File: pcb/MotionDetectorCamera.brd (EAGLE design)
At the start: 55.9 x 44.5 mm, 130 parts, among them J2 S-MOUNT-LENS-HOLDER, U1 LATTICE-ICE40HX4K-BG121, U10 NXP-NTB0102, U11 ON-NLAS3157, U12 ON-NLAS3157, U13 STM-STM32F730, U2 TI-TPS6280XYKAR, U3 MICROSD-SOCKET, U4 TI-TPS6280XYKAR, U5 W989D6DBGX6I, U6 TI-TPS63805YFFR, U8 ON-AR0330CS1C12SPKA0, U9 TI-TMUX1574, X1 SITIME-SIT8021, X2 SITIME-SIT8021

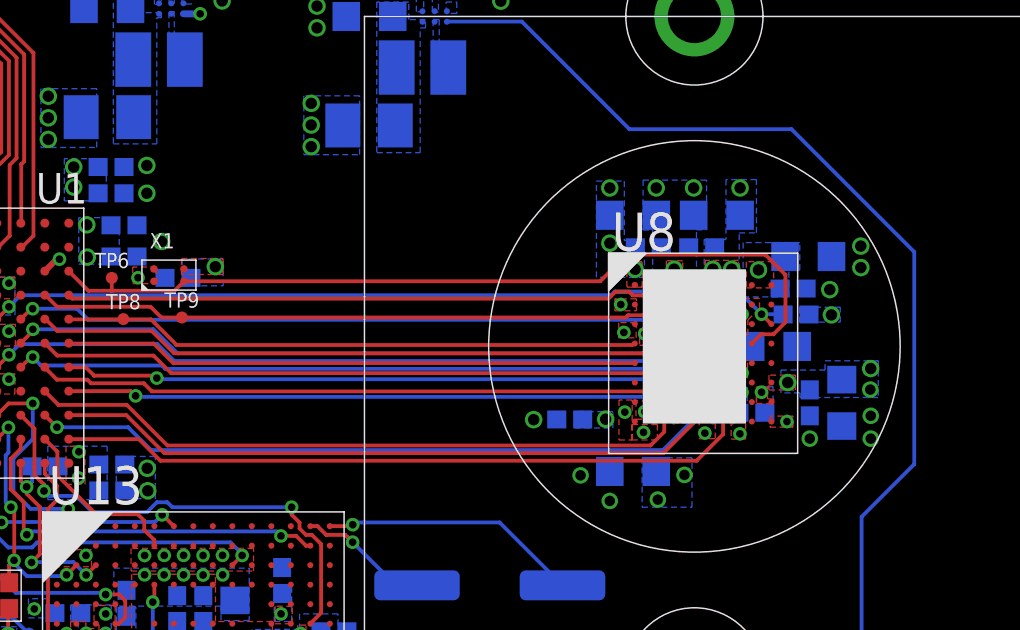
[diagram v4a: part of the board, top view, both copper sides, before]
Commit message: Add pullup for PIX_SDATA
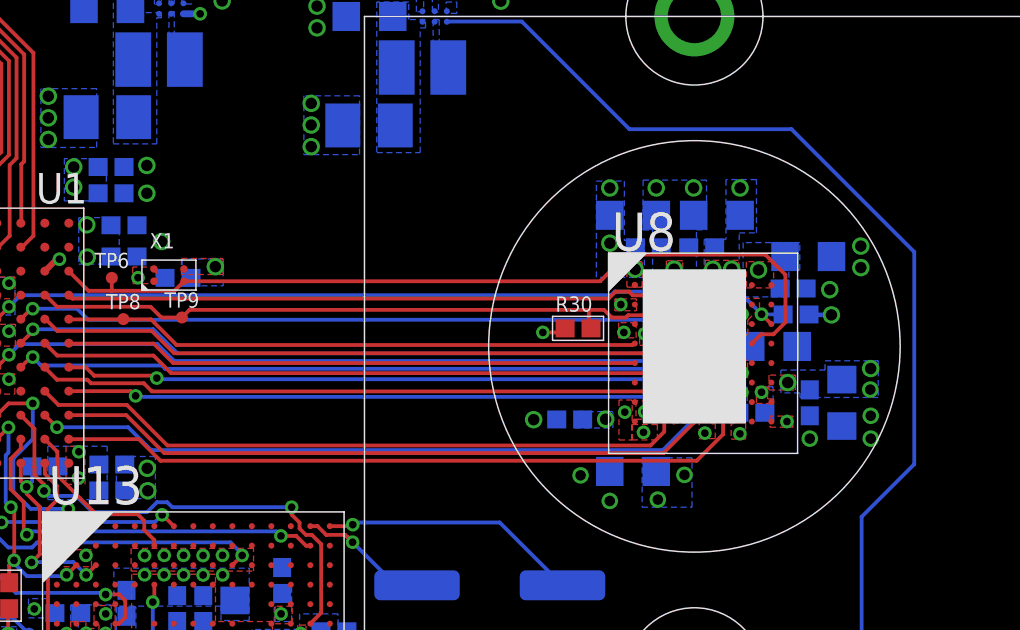
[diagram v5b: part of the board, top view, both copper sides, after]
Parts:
- added R30: 4.7k, EagleLibrary:0402
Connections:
- net 1V8: now also R30.1
- net PIX_SDATA: now also R30.2
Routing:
- net 1V8: track 4.92 -> 6.47 mm, vias 70 -> 71
- net PIX_SDATA: track 20.8 -> 21.7 mm
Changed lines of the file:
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@@
 <attribute name="PN" value="CRCW040210K0FKEDC" x="19.286221875" y="18.8950625" size="1.778" layer="27" rot="R90" display="off"/>
+</element>
+<element name="R30" library="EagleLibrary" package="0402" package3d_urn="urn:adsk.eagle:package:17080064/1" value="4.7k" x="38.249859375" y="27.805378125" smashed="yes">
+<attribute name="MFG" value="" x="38.249859375" y="27.805378125" size="1.778" layer="27" display="off"/>
+<attribute name="NAME" x="37.495859375" y="28.361378125" size="0.508" layer="25" font="vector"/>
+<attribute name="PN" value="" x="38.249859375" y="27.805378125" size="1.778" layer="27" display="off"/>
 </element>
 </elements>
@@
 </polygon>
 <polygon width="0.127" layer="16" thermals="no">
-<vertex x="45.63618125" y="28.508959375"/>
-<vertex x="45.63618125" y="28.0136625"/>
-<vertex x="46.99" y="28.0136625"/>
-<vertex x="46.99" y="28.508959375"/>
-</polygon>
-<polygon width="0.127" layer="16" thermals="no">
 <vertex x="40.386" y="23.492459375"/>
 <vertex x="40.386" y="21.844"/>
@@
 <wire x1="16.17345" y1="19.9905" x2="16.17345" y2="20.6082875" width="0.127" layer="16"/>
 <wire x1="16.17345" y1="20.6082875" x2="16.11121875" y2="20.67051875" width="0.127" layer="16"/>
+<contactref element="R30" pad="1"/>
+<wire x1="45.9493" y1="28.2702" x2="45.964540625" y2="28.254959375" width="0.1524" layer="16"/>
+<wire x1="45.964540625" y1="28.254959375" x2="46.695359375" y2="28.254959375" width="0.1524" layer="16"/>
+<via x="37.076378125" y="27.670759375" extent="1-16" drill="0.254"/>
+<wire x1="37.817359375" y1="27.805378125" x2="37.682740625" y2="27.670759375" width="0.127" layer="1"/>
+<wire x1="37.682740625" y1="27.670759375" x2="37.076378125" y2="27.670759375" width="0.127" layer="1"/>
 </signal>
 <signal name="GND">
@@
 <signal name="PIX_RST_">
 <contactref element="U8" pad="C8"/>
-<wire x1="44.693" y1="27.9498" x2="44.366178125" y2="28.276621875" width="0.127" layer="1"/>
-<wire x1="44.366178125" y1="28.27781875" x2="44.366178125" y2="28.276621875" width="0.127" layer="1"/>
 <via x="44.366178125" y="28.27781875" extent="1-16" drill="0.254"/>
 <wire x1="39.4716" y1="29.0322" x2="43.6112125" y2="29.0322" width="0.127" layer="16"/>
@@
 <wire x1="19.66468125" y1="28.91028125" x2="39.34968125" y2="28.91028125" width="0.127" layer="16"/>
 <contactref element="R23" pad="1"/>
-<wire x1="44.366178125" y1="28.27781875" x2="45.07668125" y2="28.27781875" width="0.127" layer="16"/>
-<wire x1="45.07668125" y1="28.27781875" x2="45.0843" y2="28.2702" width="0.127" layer="16"/>
+<wire x1="45.0843" y1="28.2702" x2="44.373796875" y2="28.2702" width="0.127" layer="16"/>
+<wire x1="44.373796875" y1="28.2702" x2="44.366178125" y2="28.27781875" width="0.127" layer="16"/>
+<wire x1="44.693" y1="27.9498" x2="44.366178125" y2="28.276621875" width="0.127" layer="1"/>
+<wire x1="44.366178125" y1="28.276621875" x2="44.366178125" y2="28.27781875" width="0.127" layer="1"/>
 </signal>
 <signal name="PIX_SCLK">
@@
 <contactref element="U8" pad="B2"/>
 <wire x1="39.92040625" y1="28.2419" x2="39.84710625" y2="28.1686" width="0.127" layer="1"/>
-<wire x1="39.84710625" y1="28.1686" x2="25.0444" y2="28.1686" width="0.127" layer="1"/>
+<wire x1="39.84710625" y1="28.1686" x2="39.37" y2="28.1686" width="0.127" layer="1"/>
+<wire x1="39.116" y1="28.4226" x2="38.608" y2="28.4226" width="0.127" layer="1"/>
+<wire x1="38.608" y1="28.4226" x2="25.2984" y2="28.4226" width="0.127" layer="1"/>
+<wire x1="25.2984" y1="28.4226" x2="25.0444" y2="28.1686" width="0.127" layer="1"/>
+<wire x1="39.37" y1="28.1686" x2="39.116" y2="28.4226" width="0.127" layer="1"/>
 <wire x1="25.0444" y1="28.1686" x2="24.3586" y2="28.1686" width="0.127" layer="1"/>
 <wire x1="40.793" y1="28.5998" x2="40.4351" y2="28.2419" width="0.127" layer="1"/>
@@
 <wire x1="20.8833" y1="28.5249" x2="24.0023" y2="28.5249" width="0.127" layer="1"/>
 <contactref element="TP9" pad="X"/>
+<contactref element="R30" pad="2"/>
+<wire x1="38.682359375" y1="27.805378125" x2="38.608" y2="27.8797375" width="0.127" layer="1"/>
+<wire x1="38.608" y1="27.8797375" x2="38.608" y2="28.4226" width="0.127" layer="1"/>
 </signal>
 <signal name="2V8GOOD">

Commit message: Remove 3d packages to fix ERC errors
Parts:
- C28, C29: device EagleLibrary:0805@1 -> EagleLibrary:0805

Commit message: Update TI parts with TI- prefix
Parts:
- U2, U4: device EagleLibrary:TPS6280XYKAR -> EagleLibrary:TI-TPS6280XYKAR
- U6: device EagleLibrary:TPS63805YFFR -> EagleLibrary:TI-TPS63805YFFR
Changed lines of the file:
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@@
 <attribute name="PN" value="CR0402-FX-9102GLF" x="45.936" y="8.4582" size="1.778" layer="28" rot="MR90" display="off"/>
 </element>
-<element name="U2" library="EagleLibrary" package="TPS6280XYKAR" value="TI-TPS6280XYKAR" x="24.6888" y="38.4657625" smashed="yes" rot="MR270">
+<element name="U2" library="EagleLibrary" package="TI-TPS6280XYKAR" value="TI-TPS6280XYKAR" x="24.6888" y="38.4657625" smashed="yes" rot="MR270">
 <attribute name="MFG" value="Texas Instruments" x="24.6888" y="38.4657625" size="1.778" layer="28" rot="MR270" display="off"/>
 <attribute name="NAME" x="24.992321875" y="37.939353125" size="0.508" layer="26" font="vector" rot="SMR270"/>
 <attribute name="PN" value="TPS62801YKAR" x="24.6888" y="38.4657625" size="1.778" layer="28" rot="MR270" display="off"/>
 </element>
-<element name="U4" library="EagleLibrary" package="TPS6280XYKAR" value="TI-TPS6280XYKAR" x="33.469578125" y="38.2016" smashed="yes" rot="MR270">
+<element name="U4" library="EagleLibrary" package="TI-TPS6280XYKAR" value="TI-TPS6280XYKAR" x="33.469578125" y="38.2016" smashed="yes" rot="MR270">
 <attribute name="MFG" value="Texas Instruments" x="33.469578125" y="38.2016" size="1.778" layer="28" rot="MR270" display="off"/>
 <attribute name="NAME" x="34.3515875" y="38.665140625" size="0.508" layer="26" font="vector" rot="SMR180"/>
 <attribute name="PN" value="TPS62802YKAR" x="85.539578125" y="8.9916" size="1.778" layer="28" rot="MR270" display="off"/>
 </element>
-<element name="U6" library="EagleLibrary" package="TPS63805YFFR" value="TI-TPS63805YFFR" x="48.2854" y="8.1026" smashed="yes" rot="MR180">
+<element name="U6" library="EagleLibrary" package="TI-TPS63805YFFR" value="TI-TPS63805YFFR" x="48.2854" y="8.1026" smashed="yes" rot="MR180">
 <attribute name="MFG" value="Texas Instruments" x="48.2854" y="8.1026" size="1.778" layer="28" rot="MR180" display="off"/>
 <attribute name="NAME" x="50.09898125" y="8.56668125" size="0.508" layer="26" font="vector" rot="MR270"/>
@@
 <vertex x="25.6286" y="35.9003625"/>
 </polygon>
+<wire x1="25.1423" y1="36.7639625" x2="24.6888" y2="38.2907625" width="0" layer="19" extent="16-16"/>
 </signal>
 <signal name="1V2">
@@
 <vertex x="34.460178125" y="35.6362"/>
 </polygon>
+<wire x1="33.923078125" y1="36.4998" x2="33.469578125" y2="38.0266" width="0" layer="19" extent="16-16"/>
 </signal>
 <signal name="2V8">
@@
 </polygon>
 <wire x1="48.2854" y1="7.7026" x2="48.6854" y2="7.7026" width="0.254" layer="16"/>
+<wire x1="50.7238" y1="7.2681" x2="48.6854" y2="7.7026" width="0" layer="19" extent="16-16"/>
 </signal>
 <signal name="N$13">
@@
 </polygon>
 <wire x1="48.2854" y1="8.5026" x2="48.6854" y2="8.5026" width="0.254" layer="16"/>
+<wire x1="48.6854" y1="8.5026" x2="50.7238" y2="8.9879" width="0" layer="19" extent="16-16"/>
 </signal>
 <signal name="N$11">
@@
 <vertex x="47.1424" y="9.271"/>
 </polygon>
+<wire x1="46.7996" y1="8.9655" x2="45.936" y2="8.8907" width="0" layer="19" extent="16-16"/>
 </signal>
 <signal name="GNDPLL1">

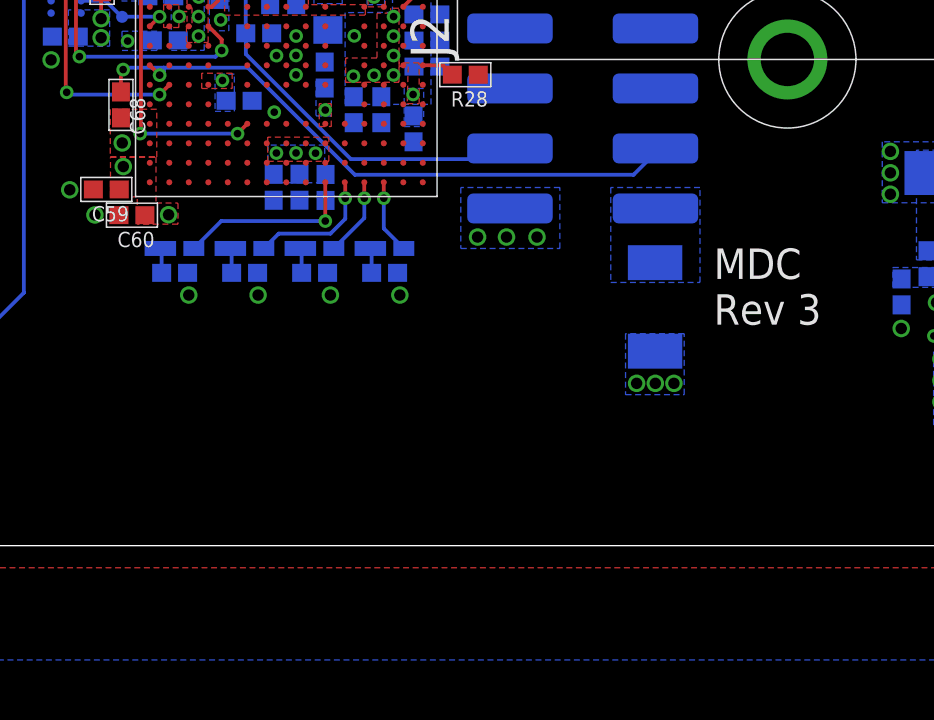
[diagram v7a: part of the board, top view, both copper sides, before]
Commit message: Added USB port, USB ESD chip, and ferrite bead
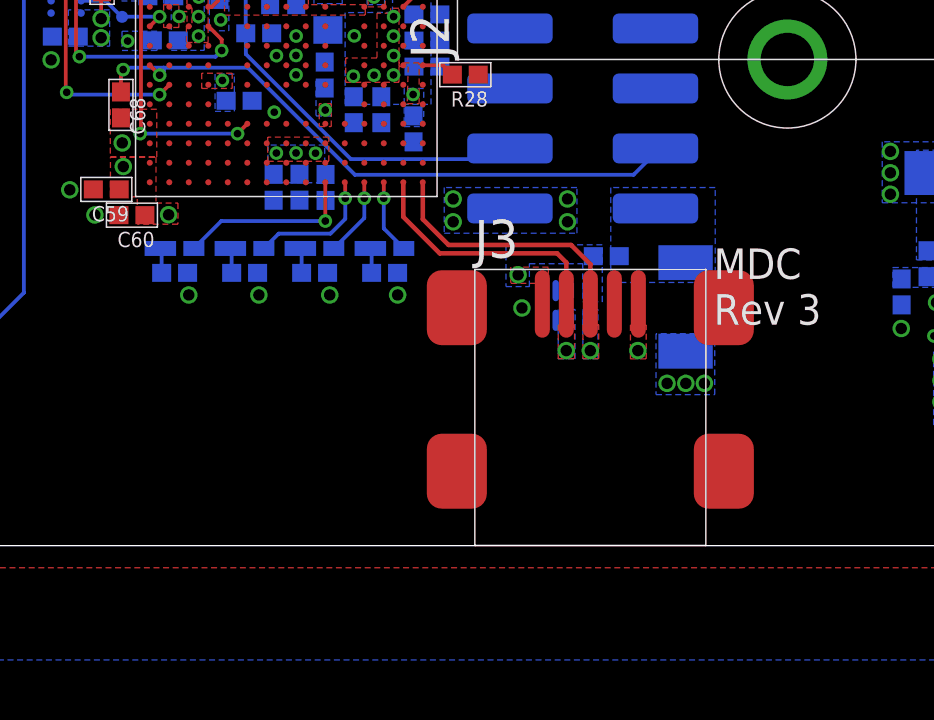
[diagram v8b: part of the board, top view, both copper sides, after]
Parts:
- added FB10: FERRITE-BEAD0402, EagleLibrary:0402
- added J3: MINI-USB-JACK, EagleLibrary:AMPHENOLFCI-10033526-N3222MLF
- added U22: TI-TPD4S012DRYR, EagleLibrary:TI-TPD4S012DRYR
- moved R1 1.02 mm to (38.7, 7.96)
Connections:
- new net N$54: FB10.1, J3.VCC, U22.6
- net GND: now also J3.GND, J3.GND2, J3.GND3, J3.GND4, J3.GND5, U22.4
- net USB_D+: now also J3.D+, U22.1
- net USB_D-: now also J3.D-, U22.2
- net VDDIN: now also FB10.2
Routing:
- net USB_D+: track 0.00 -> 8.76 mm, vias 0 -> 1
- net USB_D-: track 0.00 -> 8.60 mm, vias 0 -> 1
- net GND: vias 97 -> 100
- added copper zone on layer 1, net N$54
- added copper zone on layer 16, net N$54
- added copper zone on layer 1, net USB_D+
- added copper zone on layer 16, net USB_D+
- added copper zone on layer 1, net USB_D-
- added copper zone on layer 16, net USB_D-
